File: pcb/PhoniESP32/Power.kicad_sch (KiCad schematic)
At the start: 23 parts, among them J1 Connector, USB-TYPE-C-16P, J2 Conn_Battery, U1 TPS631000DRLR, U5 BQ24073RGTR

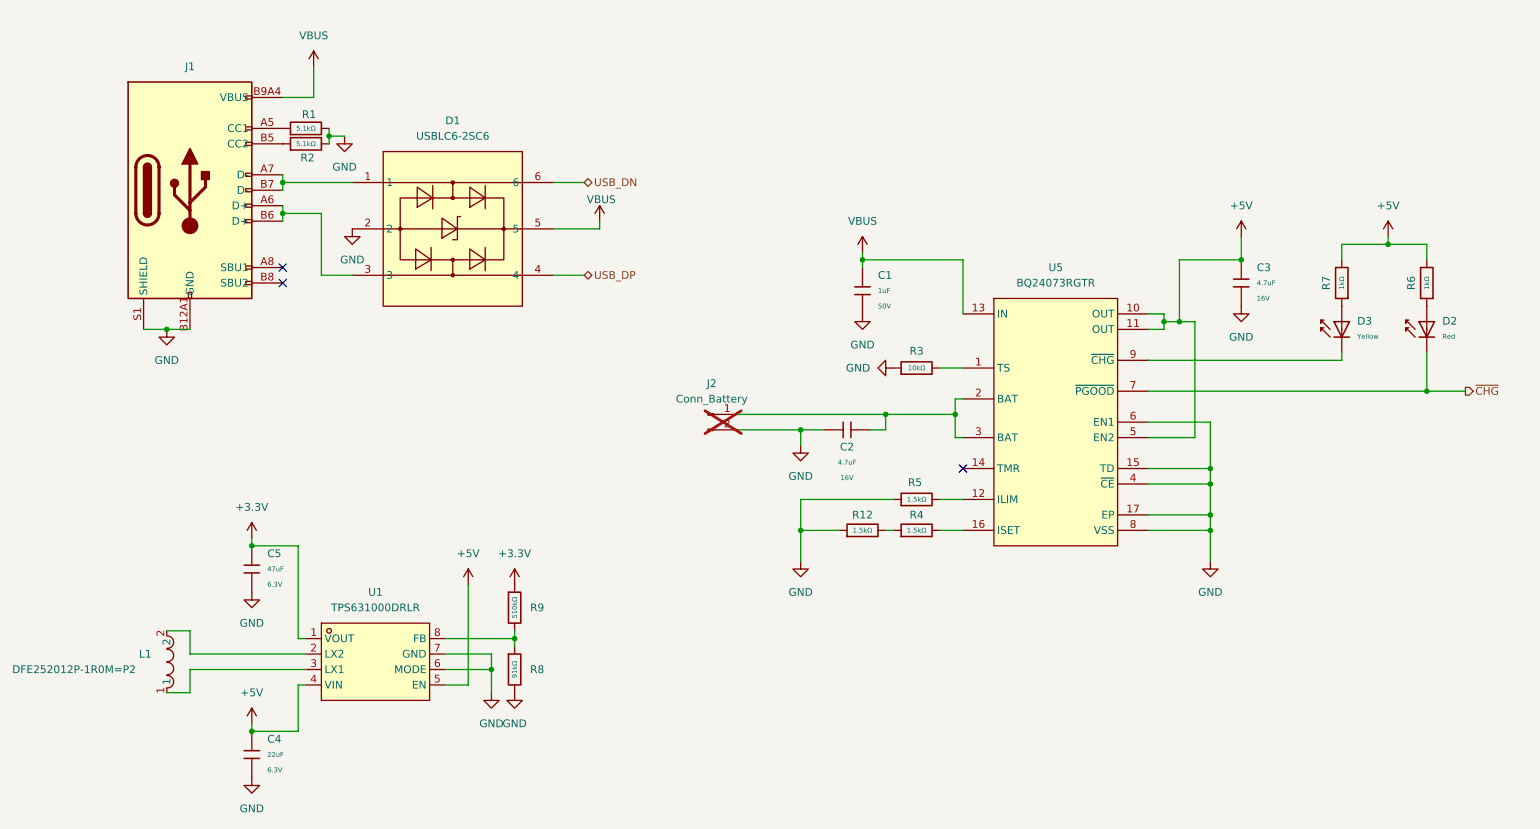
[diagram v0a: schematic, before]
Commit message: fix(pcb): add power flags for ERC
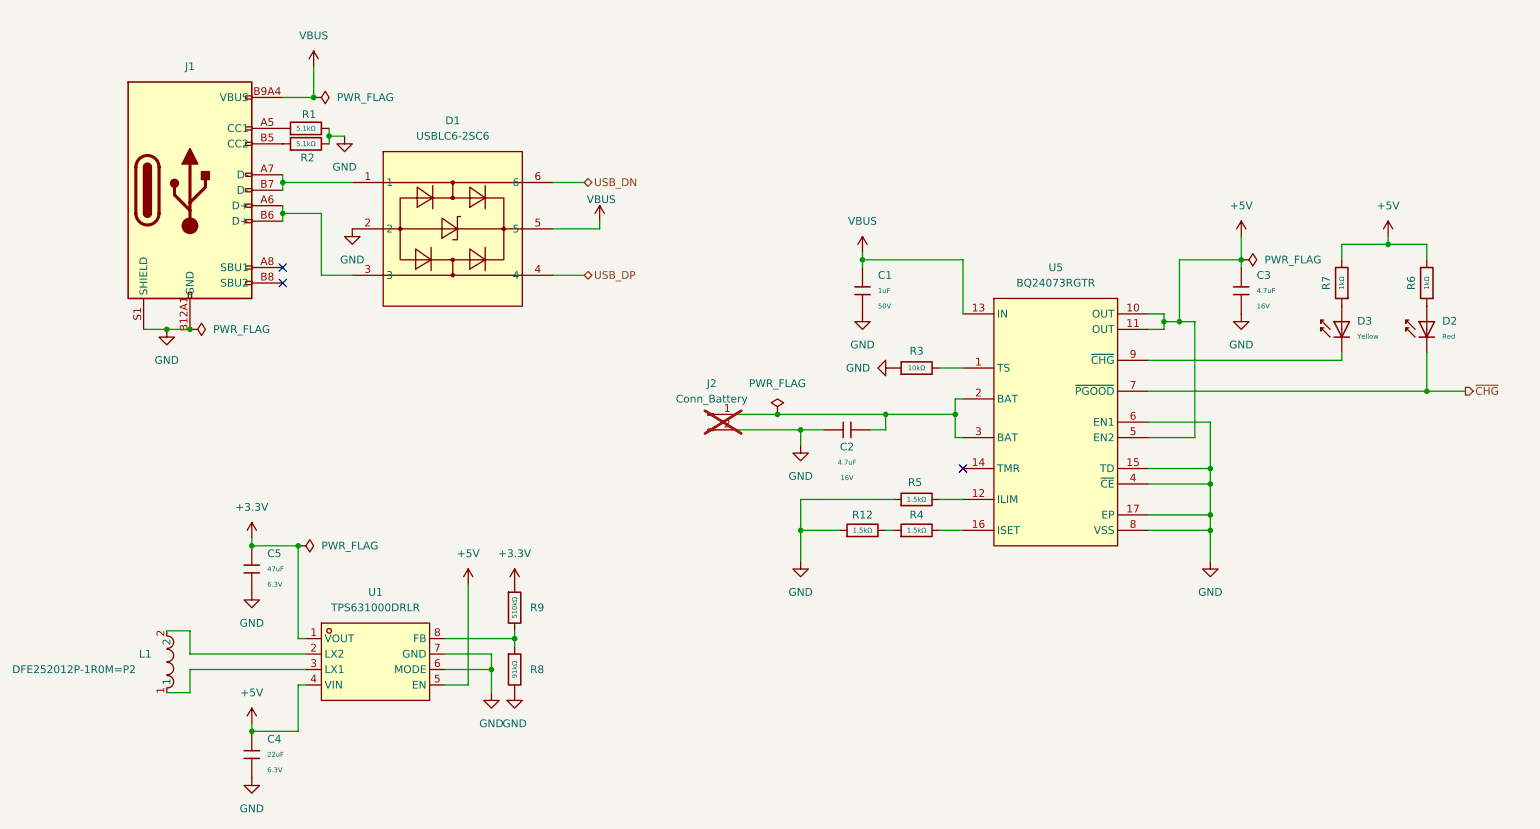
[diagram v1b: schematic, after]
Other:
- moved on the sheet: C3

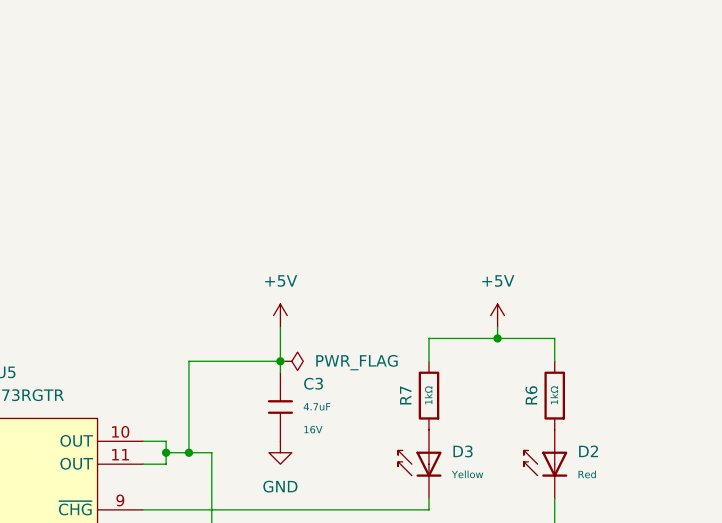
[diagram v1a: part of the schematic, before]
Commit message: feat(pcb): add power switch
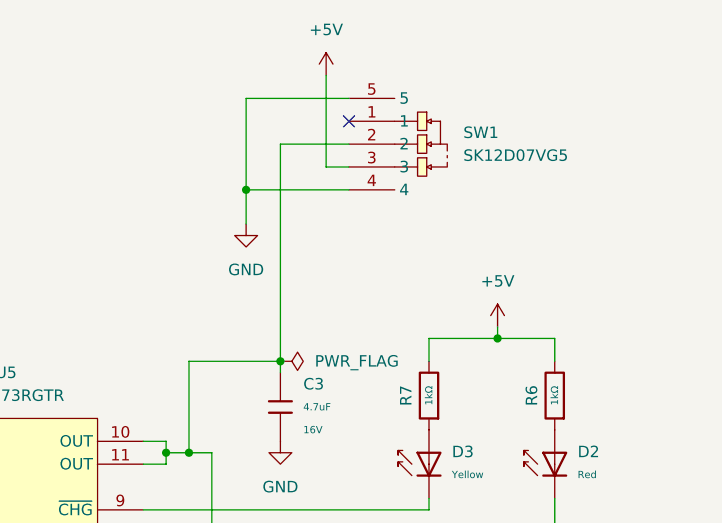
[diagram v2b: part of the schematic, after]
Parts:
- added SW1: SK12D07VG5, JLCPCB:SW-TH_SK12D07VG5-1, symbol JLCPCB:SK12D07VG5
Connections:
- net +5V: now also SW1.3; no longer C3.1, U5.10 (OUT), U5.11 (OUT), U5.5 (EN2)
- net GND: now also SW1.4, SW1.5
- new net: C3.1, SW1.2, U5.10 (OUT), U5.11 (OUT), U5.5 (EN2)
- no-connect marks 3 -> 4
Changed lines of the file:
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@@
 	)
 	(junction
+		(at 210.82 62.23)
+		(diameter 0)
+		(color 0 0 0 0)
+	)
+	(junction
 		(at 142.24 109.22)
 		(diameter 0)
@@
 		(at 168.91 115.57)
 	)
+	(no_connect
+		(at 222.25 54.61)
+	)
 	(wire
 		(pts
@@
 	(wire
 		(pts
+			(xy 210.82 52.07) (xy 210.82 62.23)
+		)
+		(stroke
+			(width 0)
+			(type default)
+		)
+	)
+	(wire
+		(pts
 			(xy 142.24 125.73) (xy 148.59 125.73)
 		)
@@
 	(wire
 		(pts
+			(xy 210.82 62.23) (xy 210.82 66.04)
+		)
+		(stroke
+			(width 0)
+			(type default)
+		)
+	)
+	(wire
+		(pts
 			(xy 59.69 143.51) (xy 60.96 143.51)
 		)
@@
 	(wire
 		(pts
-			(xy 214.63 77.47) (xy 214.63 81.28)
+			(xy 214.63 57.15) (xy 214.63 81.28)
 		)
 		(stroke
@@
 	(wire
 		(pts
+			(xy 222.25 62.23) (xy 210.82 62.23)
+		)
+		(stroke
+			(width 0)
+			(type default)
+		)
+	)
+	(wire
+		(pts
 			(xy 199.39 110.49) (xy 207.01 110.49)
 		)
@@
 	(wire
 		(pts
+			(xy 222.25 59.69) (xy 219.71 59.69)
+		)
+		(stroke
+			(width 0)
+			(type default)
+		)
+	)
+	(wire
+		(pts
 			(xy 152.4 81.28) (xy 152.4 82.55)
 		)
@@
 	(wire
 		(pts
+			(xy 219.71 49.53) (xy 219.71 59.69)
+		)
+		(stroke
+			(width 0)
+			(type default)
+		)
+	)
+	(wire
+		(pts
+			(xy 222.25 52.07) (xy 210.82 52.07)
+		)
+		(stroke
+			(width 0)
+			(type default)
+		)
+	)
+	(wire
+		(pts
 			(xy 38.1 92.71) (xy 41.91 92.71)
 		)
@@
 	(wire
 		(pts
+			(xy 222.25 57.15) (xy 214.63 57.15)
+		)
+		(stroke
+			(width 0)
+			(type default)
+		)
+	)
+	(wire
+		(pts
 			(xy 41.91 146.05) (xy 60.96 146.05)
 		)
@@
 	(symbol
 		(lib_id "power:+5V")
-		(at 214.63 77.47 0)
+		(at 219.71 49.53 0)
 		(unit 1)
 		(exclude_from_sim no)
@@
 		(fields_autoplaced yes)
 		(property "Reference" "#PWR010"
-			(at 214.63 81.28 0)
+			(at 219.71 53.34 0)
 			(effects
 				(font
@@
 		)
 		(property "Value" "+5V"
-			(at 214.63 72.39 0)
+			(at 219.71 44.45 0)
 			(effects
 				(font
@@
 		)
 		(property "Footprint" ""
-			(at 214.63 77.47 0)
+			(at 219.71 49.53 0)
 			(effects
 				(font
@@
 		)
 		(property "Datasheet" ""
-			(at 214.63 77.47 0)
+			(at 219.71 49.53 0)
 			(effects
 				(font
@@
 		)
 		(property "Description" "Power symbol creates a global label with name \"+5V\""
-			(at 214.63 77.47 0)
+			(at 219.71 49.53 0)
 			(effects
 				(font
@@
 	(symbol
 		(lib_id "power:GND")
+		(at 210.82 66.04 0)
+		(unit 1)
+		(exclude_from_sim no)
+		(in_bom yes)
+		(on_board yes)
+		(dnp no)
+		(fields_autoplaced yes)
+		(property "Reference" "#PWR022"
+			(at 210.82 72.39 0)
+			(effects
+				(font
+					(size 1.27 1.27)
+				)
+				(hide yes)
+			)
+		)
+		(property "Value" "GND"
+			(at 210.82 71.12 0)
+			(effects
+				(font
+					(size 1.27 1.27)
+				)
+			)
+		)
+		(property "Footprint" ""
+			(at 210.82 66.04 0)
+			(effects
+				(font
+					(size 1.27 1.27)
+				)
+				(hide yes)
+			)
+		)
+		(property "Datasheet" ""
+			(at 210.82 66.04 0)
+			(effects
+				(font
+					(size 1.27 1.27)
+				)
+				(hide yes)
+			)
+		)
+		(property "Description" "Power symbol creates a global label with name \"GND\" , ground"
+			(at 210.82 66.04 0)
+			(effects
+				(font
+					(size 1.27 1.27)
+				)
+				(hide yes)
+			)
+		)
+		(pin "1"
+		)
+		(instances
+			(project ""
+				(path "/a246d5c1-33d2-4ce4-8f5f-6a6b3acd3d9a/962bc92e-62d4-464b-8dbf-0ffa43f94661"
+					(reference "#PWR022")
+					(unit 1)
+				)
+			)
+		)
+	)
+	(symbol
+		(lib_id "power:GND")
 		(at 91.44 152.4 0)
 		(unit 1)
@@
 					(unit 1)
 				)
+			)
+		)
+	)
+	(symbol
+		(lib_id "JLCPCB:SK12D07VG5")
+		(at 227.33 57.15 270)
+		(unit 1)
+		(exclude_from_sim no)
+		(in_bom yes)
+		(on_board yes)
+		(dnp no)
+		(fields_autoplaced yes)
+		(property "Reference" "SW1"
+			(at 234.95 55.8799 90)
+			(effects
+				(font
+					(size 1.27 1.27)
+				)
+				(justify left)
+			)
+		)
+		(property "Value" "SK12D07VG5"
+			(at 234.95 58.4199 90)
+			(effects
+				(font
+					(size 1.27 1.27)
+				)
+				(justify left)
+			)
+		)
+		(property "Footprint" "JLCPCB:SW-TH_SK12D07VG5-1"
+			(at 214.63 57.15 0)
+			(effects
+				(font
+					(size 1.27 1.27)
+				)
+				(hide yes)
+			)
+		)
+		(property "Datasheet" "https://lcsc.com/product-detail/Toggle-Switches_SHOU-HAN-SK12D07VG5_C431548.html"
+			(at 212.09 57.15 0)
+			(effects
+				(font
+					(size 1.27 1.27)
+				)
+				(hide yes)
+			)
+		)
+		(property "Description" ""
+			(at 227.33 57.15 0)
+			(effects
+				(font
+					(size 1.27 1.27)
+				)
+				(hide yes)
+			)
+		)
+		(property "LCSC Part" "C431548"
+			(at 209.55 57.15 0)
+			(effects
+				(font
+					(size 1.27 1.27)
+				)
+				(hide yes)
+			)
+		)
+		(pin "3"
+		)
+		(pin "2"
+		)
+		(pin "1"
+		)
+		(pin "5"
+		)
+		(pin "4"
+		)
+		(instances
+			(project ""
+				(path "/a246d5c1-33d2-4ce4-8f5f-6a6b3acd3d9a/962bc92e-62d4-464b-8dbf-0ffa43f94661"
+					(reference "SW1")
+					(unit 1)
+				)

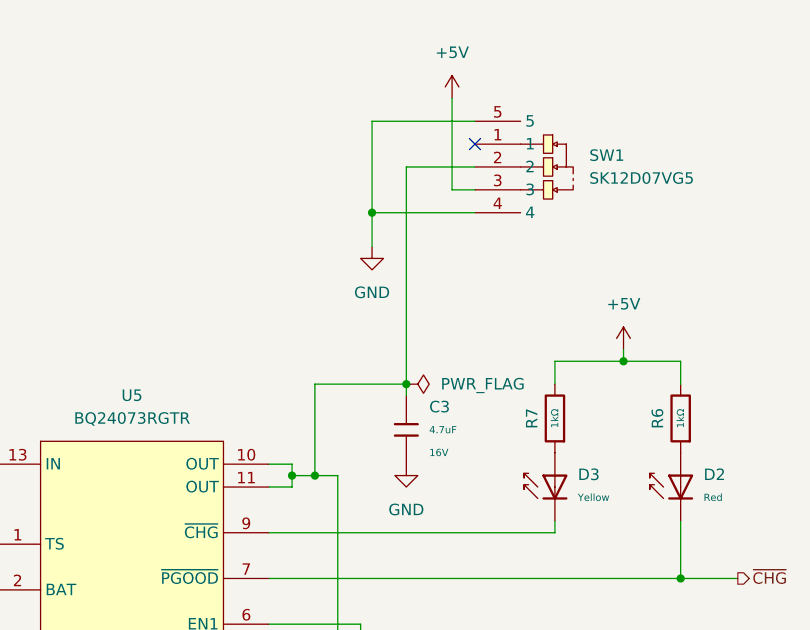
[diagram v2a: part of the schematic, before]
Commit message: fix(pcb): add 22 Ohm resistors on USB data lines
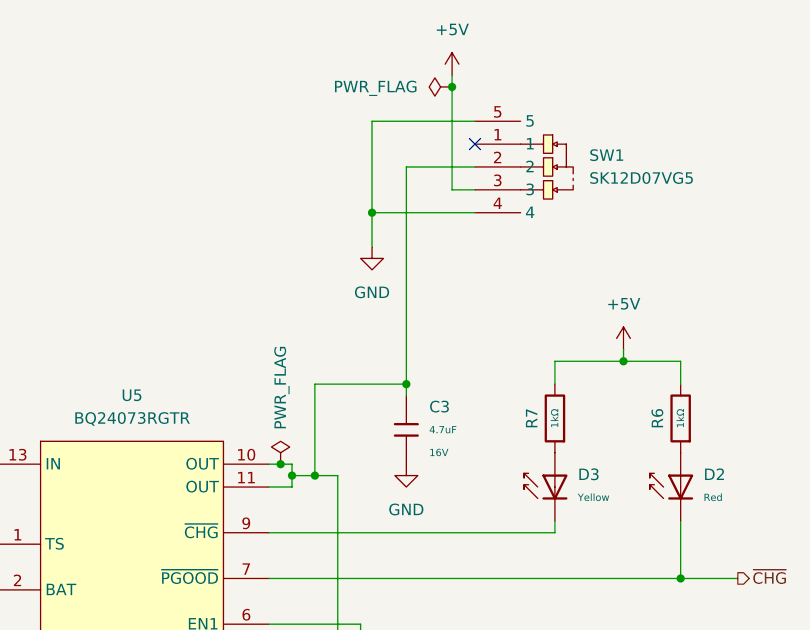
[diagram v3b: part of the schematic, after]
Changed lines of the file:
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@@
 	)
 	(junction
+		(at 200.66 90.17)
+		(diameter 0)
+		(color 0 0 0 0)
+	)
+	(junction
 		(at 95.25 143.51)
 		(diameter 0)
@@
 	)
 	(junction
+		(at 219.71 48.26)
+		(diameter 0)
+		(color 0 0 0 0)
+	)
+	(junction
 		(at 142.24 125.73)
 		(diameter 0)
@@
 	(wire
 		(pts
+			(xy 219.71 48.26) (xy 219.71 59.69)
+		)
+		(stroke
+			(width 0)
+			(type default)
+		)
+	)
+	(wire
+		(pts
 			(xy 52.07 157.48) (xy 52.07 158.75)
 		)
@@
 	(wire
 		(pts
-			(xy 199.39 90.17) (xy 201.93 90.17)
+			(xy 199.39 90.17) (xy 200.66 90.17)
 		)
 		(stroke
@@
 	(wire
 		(pts
-			(xy 219.71 49.53) (xy 219.71 59.69)
+			(xy 222.25 52.07) (xy 210.82 52.07)
 		)
 		(stroke
@@
 	(wire
 		(pts
-			(xy 222.25 52.07) (xy 210.82 52.07)
+			(xy 38.1 92.71) (xy 41.91 92.71)
 		)
 		(stroke
@@
 	(wire
 		(pts
-			(xy 38.1 92.71) (xy 41.91 92.71)
+			(xy 200.66 90.17) (xy 201.93 90.17)
 		)
 		(stroke
@@
 	(wire
 		(pts
+			(xy 219.71 46.99) (xy 219.71 48.26)
+		)
+		(stroke
+			(width 0)
+			(type default)
+		)
+	)
+	(wire
+		(pts
 			(xy 209.55 115.57) (xy 209.55 118.11)
 		)
@@
 	)
 	(symbol
+		(lib_id "power:PWR_FLAG")
+		(at 200.66 90.17 0)
+		(unit 1)
+		(exclude_from_sim no)
+		(in_bom yes)
+		(on_board yes)
+		(dnp no)
+		(property "Reference" "#FLG06"
+			(at 200.66 88.265 0)
+			(effects
+				(font
+					(size 1.27 1.27)
+				)
+				(hide yes)
+			)
+		)
+		(property "Value" "PWR_FLAG"
+			(at 200.6601 86.36 90)
+			(effects
+				(font
+					(size 1.27 1.27)
+				)
+				(justify left)
+			)
+		)
+		(property "Footprint" ""
+			(at 200.66 90.17 0)
+			(effects
+				(font
+					(size 1.27 1.27)
+				)
+				(hide yes)
+			)
+		)
+		(property "Datasheet" "~"
+			(at 200.66 90.17 0)
+			(effects
+				(font
+					(size 1.27 1.27)
+				)
+				(hide yes)
+			)
+		)
+		(property "Description" "Special symbol for telling ERC where power comes from"
+			(at 200.66 90.17 0)
+			(effects
+				(font
+					(size 1.27 1.27)
+				)
+				(hide yes)
+			)
+		)
+		(pin "1"
+		)
+		(instances
+			(project "PhoniESP32"
+				(path "/a246d5c1-33d2-4ce4-8f5f-6a6b3acd3d9a/962bc92e-62d4-464b-8dbf-0ffa43f94661"
+					(reference "#FLG06")
+					(unit 1)
+				)
+			)
+		)
+	)
+	(symbol
 		(lib_id "PCM_JLCPCB-Resistors:0603,1.5kΩ")
 		(at 161.29 125.73 90)
@@
 	(symbol
 		(lib_id "power:PWR_FLAG")
-		(at 214.63 81.28 270)
+		(at 219.71 48.26 90)
 		(unit 1)
 		(exclude_from_sim no)
@@
 		(fields_autoplaced yes)
 		(property "Reference" "#FLG04"
-			(at 216.535 81.28 0)
+			(at 217.805 48.26 0)
 			(effects
 				(font
@@
 		)
 		(property "Value" "PWR_FLAG"
-			(at 218.44 81.2799 90)
+			(at 215.9 48.2599 90)
 			(effects
 				(font
@@
 		)
 		(property "Footprint" ""
-			(at 214.63 81.28 0)
+			(at 219.71 48.26 0)
 			(effects
 				(font
@@
 		)
 		(property "Datasheet" "~"
-			(at 214.63 81.28 0)
+			(at 219.71 48.26 0)
 			(effects
 				(font
@@
 		)
 		(property "Description" "Special symbol for telling ERC where power comes from"
-			(at 214.63 81.28 0)
+			(at 219.71 48.26 0)
 			(effects
 				(font
@@
 	(symbol
 		(lib_id "power:+5V")
-		(at 219.71 49.53 0)
+		(at 219.71 46.99 0)
 		(unit 1)
 		(exclude_from_sim no)
@@
 		(on_board yes)
 		(dnp no)
-		(fields_autoplaced yes)
 		(property "Reference" "#PWR010"
-			(at 219.71 53.34 0)
+			(at 219.71 50.8 0)
 			(effects
 				(font
@@
 		)
 		(property "Value" "+5V"
-			(at 219.71 44.45 0)
+			(at 219.71 41.91 0)
 			(effects
 				(font
@@
 		)
 		(property "Footprint" ""
-			(at 219.71 49.53 0)
+			(at 219.71 46.99 0)
 			(effects
 				(font
@@
 		)
 		(property "Datasheet" ""
-			(at 219.71 49.53 0)
+			(at 219.71 46.99 0)
 			(effects
 				(font
@@
 		)
 		(property "Description" "Power symbol creates a global label with name \"+5V\""
-			(at 219.71 49.53 0)
+			(at 219.71 46.99 0)
 			(effects
 				(font

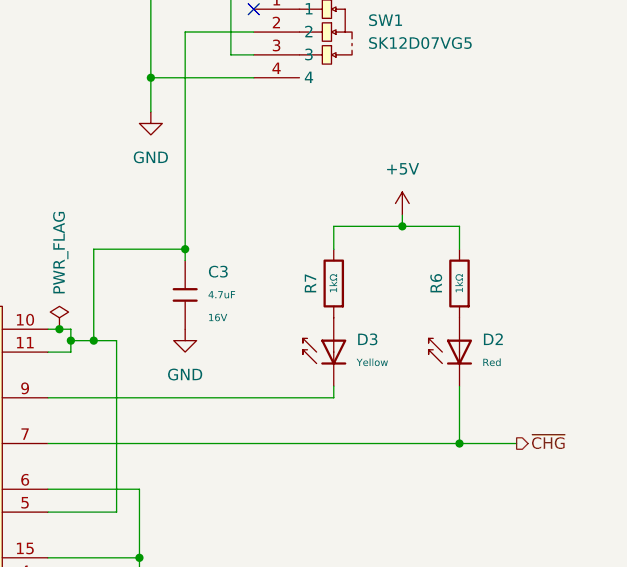
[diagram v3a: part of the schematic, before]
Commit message: chore(pcb): make charging indicator LEDs brighter
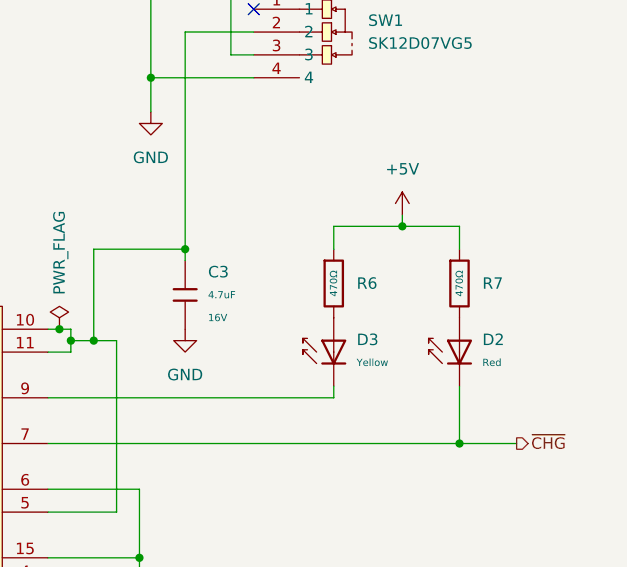
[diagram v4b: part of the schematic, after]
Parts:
- removed R6, R7: 1kΩ, PCM_JLCPCB:R_0603, symbol PCM_JLCPCB-Resistors:0603,1kΩ
- added R6, R7: 470Ω, PCM_JLCPCB:R_0603, symbol PCM_JLCPCB-Resistors:0603,470Ω
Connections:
- net +5V: now also R6.1, R7.1
- net at D2.2: now also R7.2
- net at D3.2: now also R6.2

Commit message: feat(pcb): place test points and placeholders
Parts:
- added R19: 47kΩ, PCM_JLCPCB:R_0603, symbol PCM_JLCPCB-Resistors:0603,47kΩ
- added R20: 0Ω, PCM_JLCPCB:R_0603, symbol PCM_JLCPCB-Resistors:0603,0Ω
- added TP1, TP2, TP4, TP5: TestPoint, TestPoint:TestPoint_Pad_D1.0mm, symbol Connector:TestPoint
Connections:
- net +3.3V: now also TP4.1
- net GND: now also R19.1, R20.2, TP2.1; no longer U5.15 (TD)
- net VBUS: now also TP1.1
- net at C3.1, SW1.2, U5.10 (OUT)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: now also TP5.1
- net at U5.14 (TMR): now also R19.2
- new net: R20.1, U5.15 (TD)
- no-connect marks 4 -> 3

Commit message: feat(pcb): initial traces
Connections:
- net D-: now reaches D1.1, J1.A7 (D-), J1.B7 (D-)
- net D+: now reaches D1.3, J1.A6 (D+), J1.B6 (D+)
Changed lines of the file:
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@@
+		)
+	)
+	(label "D+"
+		(at 57.15 73.66 0)
+		(effects
+			(font
+				(size 1.27 1.27)
+			)
+			(justify left bottom)
+		)
+	)
+	(label "D-"
+		(at 57.15 68.58 0)
+		(effects
+			(font
+				(size 1.27 1.27)
+			)
+			(justify left bottom)
 		)
 	)
